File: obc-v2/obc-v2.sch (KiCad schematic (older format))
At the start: 57 parts

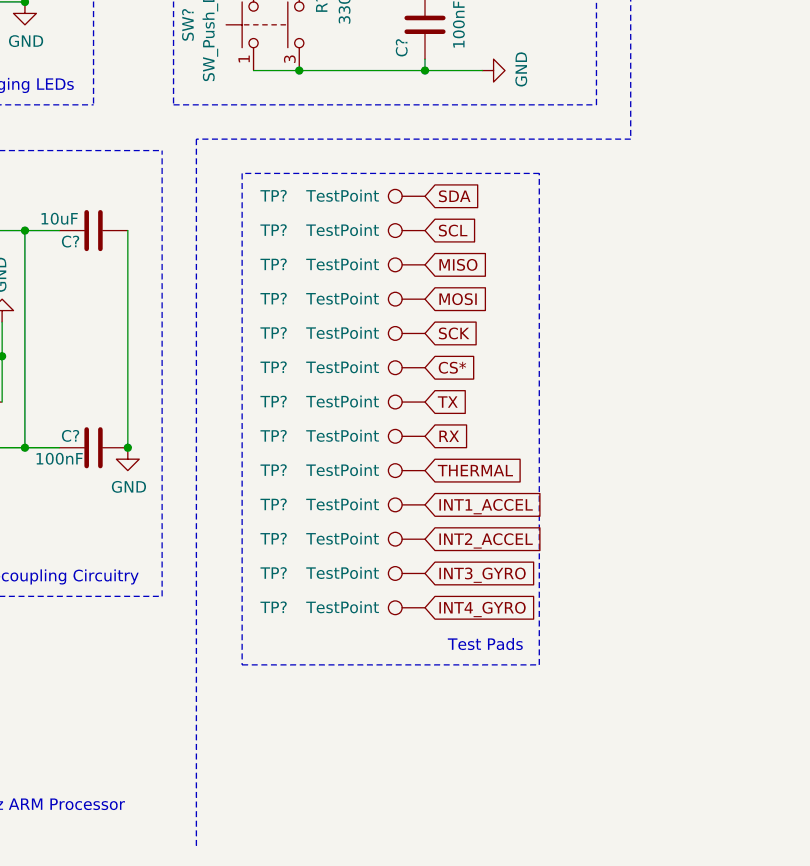
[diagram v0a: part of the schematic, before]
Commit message: obc-v2: Add test pads
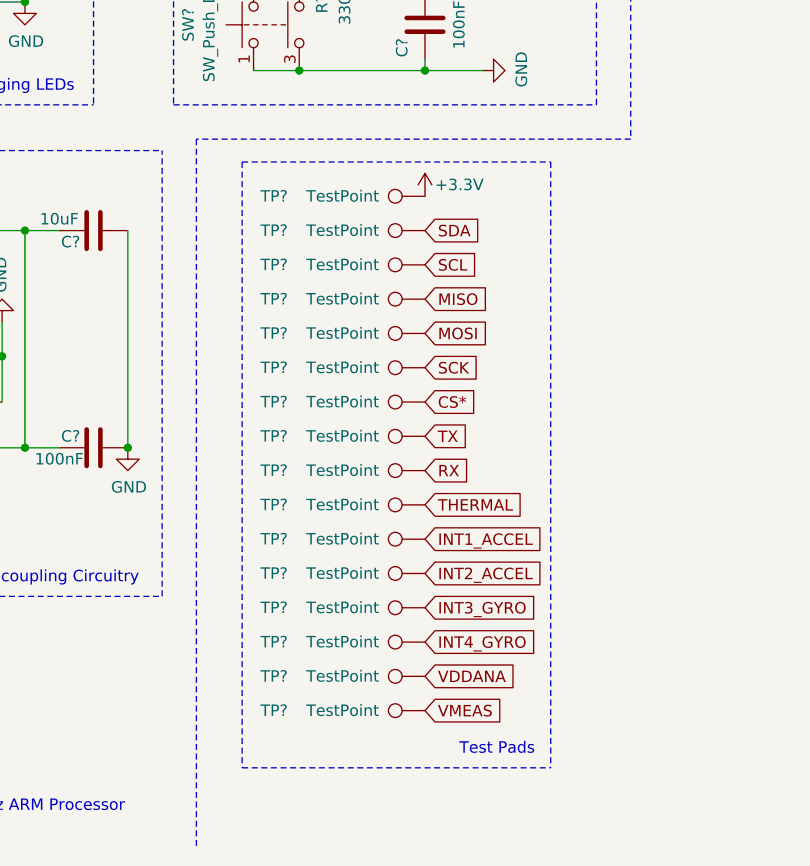
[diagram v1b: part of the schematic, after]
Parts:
- added TP? (x3): TestPoint, symbol Connector:TestPoint
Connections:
- net +3V3: now also TP?.1
- net VDDANA: now also TP?.1
- net VMEAS: now also TP?.1
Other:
- moved on the sheet: TP?
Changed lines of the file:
@@
 L Connector:TestPoint TP?
 U 1 1 6165481C
+P 4200 5100
+F 0 "TP?" V 4200 5700 50  0000 L CNN
+F 1 "TestPoint" V 4200 5300 50  0000 L CNN
+F 2 "" H 4400 5100 50  0001 C CNN
+F 3 "" H 4400 5100 50  0001 C CNN
+	1    4200 5100
+	0    -1   -1   0
+$EndComp
+Text GLabel 4200 5100 2    50   Input ~ 0
+SDA
+$Comp
+L Connector:TestPoint TP?
+U 1 1 616A4E70
+P 4200 5250
+F 0 "TP?" V 4200 5850 50  0000 L CNN
+F 1 "TestPoint" V 4200 5450 50  0000 L CNN
+F 2 "" H 4400 5250 50  0001 C CNN
+F 3 "" H 4400 5250 50  0001 C CNN
+	1    4200 5250
+	0    -1   -1   0
+$EndComp
+Text GLabel 4200 5250 2    50   Input ~ 0
+SCL
+$Comp
+L Connector:TestPoint TP?
+U 1 1 616A8E8A
+P 4200 5400
+F 0 "TP?" V 4200 6000 50  0000 L CNN
+F 1 "TestPoint" V 4200 5600 50  0000 L CNN
+F 2 "" H 4400 5400 50  0001 C CNN
+F 3 "" H 4400 5400 50  0001 C CNN
+	1    4200 5400
+	0    -1   -1   0
+$EndComp
+Text GLabel 4200 5400 2    50   Input ~ 0
+MISO
+$Comp
+L Connector:TestPoint TP?
+U 1 1 616A8E91
+P 4200 5550
+F 0 "TP?" V 4200 6150 50  0000 L CNN
+F 1 "TestPoint" V 4200 5750 50  0000 L CNN
+F 2 "" H 4400 5550 50  0001 C CNN
+F 3 "" H 4400 5550 50  0001 C CNN
+	1    4200 5550
+	0    -1   -1   0
+$EndComp
+Text GLabel 4200 5550 2    50   Input ~ 0
+MOSI
+$Comp
+L Connector:TestPoint TP?
+U 1 1 616AD625
+P 4200 5700
+F 0 "TP?" V 4200 6300 50  0000 L CNN
+F 1 "TestPoint" V 4200 5900 50  0000 L CNN
+F 2 "" H 4400 5700 50  0001 C CNN
+F 3 "" H 4400 5700 50  0001 C CNN
+	1    4200 5700
+	0    -1   -1   0
+$EndComp
+Text GLabel 4200 5700 2    50   Input ~ 0
+SCK
+$Comp
+L Connector:TestPoint TP?
+U 1 1 616AD62C
+P 4200 5850
+F 0 "TP?" V 4200 6450 50  0000 L CNN
+F 1 "TestPoint" V 4200 6050 50  0000 L CNN
+F 2 "" H 4400 5850 50  0001 C CNN
+F 3 "" H 4400 5850 50  0001 C CNN
+	1    4200 5850
+	0    -1   -1   0
+$EndComp
+Text GLabel 4200 5850 2    50   Input ~ 0
+CS*
+$Comp
+L Connector:TestPoint TP?
+U 1 1 616AD633
+P 4200 6000
+F 0 "TP?" V 4200 6600 50  0000 L CNN
+F 1 "TestPoint" V 4200 6200 50  0000 L CNN
+F 2 "" H 4400 6000 50  0001 C CNN
+F 3 "" H 4400 6000 50  0001 C CNN
+	1    4200 6000
+	0    -1   -1   0
+$EndComp
+Text GLabel 4200 6000 2    50   Input ~ 0
+TX
+$Comp
+L Connector:TestPoint TP?
+U 1 1 616AD63A
+P 4200 6150
+F 0 "TP?" V 4200 6750 50  0000 L CNN
+F 1 "TestPoint" V 4200 6350 50  0000 L CNN
+F 2 "" H 4400 6150 50  0001 C CNN
+F 3 "" H 4400 6150 50  0001 C CNN
+	1    4200 6150
+	0    -1   -1   0
+$EndComp
+Text GLabel 4200 6150 2    50   Input ~ 0
+RX
+$Comp
+L Connector:TestPoint TP?
+U 1 1 616B2BB2
+P 4200 6300
+F 0 "TP?" V 4200 6900 50  0000 L CNN
+F 1 "TestPoint" V 4200 6500 50  0000 L CNN
+F 2 "" H 4400 6300 50  0001 C CNN
+F 3 "" H 4400 6300 50  0001 C CNN
+	1    4200 6300
+	0    -1   -1   0
+$EndComp
+Text GLabel 4200 6300 2    50   Input ~ 0
+THERMAL
+$Comp
+L Connector:TestPoint TP?
+U 1 1 616B2BB9
+P 4200 6450
+F 0 "TP?" V 4200 7050 50  0000 L CNN
+F 1 "TestPoint" V 4200 6650 50  0000 L CNN
+F 2 "" H 4400 6450 50  0001 C CNN
+F 3 "" H 4400 6450 50  0001 C CNN
+	1    4200 6450
+	0    -1   -1   0
+$EndComp
+Text GLabel 4200 6450 2    50   Input ~ 0
+INT1_ACCEL
+$Comp
+L Connector:TestPoint TP?
+U 1 1 616B2BC0
+P 4200 6600
+F 0 "TP?" V 4200 7200 50  0000 L CNN
+F 1 "TestPoint" V 4200 6800 50  0000 L CNN
+F 2 "" H 4400 6600 50  0001 C CNN
+F 3 "" H 4400 6600 50  0001 C CNN
+	1    4200 6600
+	0    -1   -1   0
+$EndComp
+Text GLabel 4200 6600 2    50   Input ~ 0
+INT2_ACCEL
+$Comp
+L Connector:TestPoint TP?
+U 1 1 616B2BC7
+P 4200 6750
+F 0 "TP?" V 4200 7350 50  0000 L CNN
+F 1 "TestPoint" V 4200 6950 50  0000 L CNN
+F 2 "" H 4400 6750 50  0001 C CNN
+F 3 "" H 4400 6750 50  0001 C CNN
+	1    4200 6750
+	0    -1   -1   0
+$EndComp
+Text GLabel 4200 6750 2    50   Input ~ 0
+INT3_GYRO
+$Comp
+L Connector:TestPoint TP?
+U 1 1 616B2BCE
+P 4200 6900
+F 0 "TP?" V 4200 7500 50  0000 L CNN
+F 1 "TestPoint" V 4200 7100 50  0000 L CNN
+F 2 "" H 4400 6900 50  0001 C CNN
+F 3 "" H 4400 6900 50  0001 C CNN
+	1    4200 6900
+	0    -1   -1   0
+$EndComp
+Text GLabel 4200 6900 2    50   Input ~ 0
+INT4_GYRO
+Text Notes 4350 7400 0    50   ~ 0
+Test Pads
+$Comp
+L Connector:TestPoint TP?
+U 1 1 61552B8D
 P 4200 4950
 F 0 "TP?" V 4200 5550 50  0000 L CNN
@@
 	0    -1   -1   0
 $EndComp
-Text GLabel 4200 4950 2    50   Input ~ 0
-SDA
-$Comp
-L Connector:TestPoint TP?
-U 1 1 616A4E70
-P 4200 5100
-F 0 "TP?" V 4200 5700 50  0000 L CNN
-F 1 "TestPoint" V 4200 5300 50  0000 L CNN
-F 2 "" H 4400 5100 50  0001 C CNN
-F 3 "" H 4400 5100 50  0001 C CNN
-	1    4200 5100
-	0    -1   -1   0
-$EndComp
-Text GLabel 4200 5100 2    50   Input ~ 0
-SCL
-$Comp
-L Connector:TestPoint TP?
-U 1 1 616A8E8A
-P 4200 5250
-F 0 "TP?" V 4200 5850 50  0000 L CNN
-F 1 "TestPoint" V 4200 5450 50  0000 L CNN
-F 2 "" H 4400 5250 50  0001 C CNN
-F 3 "" H 4400 5250 50  0001 C CNN
-	1    4200 5250
-	0    -1   -1   0
-$EndComp
-Text GLabel 4200 5250 2    50   Input ~ 0
-MISO
-$Comp
-L Connector:TestPoint TP?
-U 1 1 616A8E91
-P 4200 5400
-F 0 "TP?" V 4200 6000 50  0000 L CNN
-F 1 "TestPoint" V 4200 5600 50  0000 L CNN
-F 2 "" H 4400 5400 50  0001 C CNN
-F 3 "" H 4400 5400 50  0001 C CNN
-	1    4200 5400
-	0    -1   -1   0
-$EndComp
-Text GLabel 4200 5400 2    50   Input ~ 0
-MOSI
-$Comp
-L Connector:TestPoint TP?
-U 1 1 616AD625
-P 4200 5550
-F 0 "TP?" V 4200 6150 50  0000 L CNN
-F 1 "TestPoint" V 4200 5750 50  0000 L CNN
-F 2 "" H 4400 5550 50  0001 C CNN
-F 3 "" H 4400 5550 50  0001 C CNN
-	1    4200 5550
-	0    -1   -1   0
-$EndComp
-Text GLabel 4200 5550 2    50   Input ~ 0
-SCK
-$Comp
-L Connector:TestPoint TP?
-U 1 1 616AD62C
-P 4200 5700
-F 0 "TP?" V 4200 6300 50  0000 L CNN
-F 1 "TestPoint" V 4200 5900 50  0000 L CNN
-F 2 "" H 4400 5700 50  0001 C CNN
-F 3 "" H 4400 5700 50  0001 C CNN
-	1    4200 5700
-	0    -1   -1   0
-$EndComp
-Text GLabel 4200 5700 2    50   Input ~ 0
-CS*
-$Comp
-L Connector:TestPoint TP?
-U 1 1 616AD633
-P 4200 5850
-F 0 "TP?" V 4200 6450 50  0000 L CNN
-F 1 "TestPoint" V 4200 6050 50  0000 L CNN
-F 2 "" H 4400 5850 50  0001 C CNN
-F 3 "" H 4400 5850 50  0001 C CNN
-	1    4200 5850
-	0    -1   -1   0
-$EndComp
-Text GLabel 4200 5850 2    50   Input ~ 0
-TX
-$Comp
-L Connector:TestPoint TP?
-U 1 1 616AD63A
-P 4200 6000
-F 0 "TP?" V 4200 6600 50  0000 L CNN
-F 1 "TestPoint" V 4200 6200 50  0000 L CNN
-F 2 "" H 4400 6000 50  0001 C CNN
-F 3 "" H 4400 6000 50  0001 C CNN
-	1    4200 6000
-	0    -1   -1   0
-$EndComp
-Text GLabel 4200 6000 2    50   Input ~ 0
-RX
-$Comp
-L Connector:TestPoint TP?
-U 1 1 616B2BB2
-P 4200 6150
-F 0 "TP?" V 4200 6750 50  0000 L CNN
-F 1 "TestPoint" V 4200 6350 50  0000 L CNN
-F 2 "" H 4400 6150 50  0001 C CNN
-F 3 "" H 4400 6150 50  0001 C CNN
-	1    4200 6150
-	0    -1   -1   0
-$EndComp
-Text GLabel 4200 6150 2    50   Input ~ 0
-THERMAL
-$Comp
-L Connector:TestPoint TP?
-U 1 1 616B2BB9
-P 4200 6300
-F 0 "TP?" V 4200 6900 50  0000 L CNN
-F 1 "TestPoint" V 4200 6500 50  0000 L CNN
-F 2 "" H 4400 6300 50  0001 C CNN
-F 3 "" H 4400 6300 50  0001 C CNN
-	1    4200 6300
-	0    -1   -1   0
-$EndComp
-Text GLabel 4200 6300 2    50   Input ~ 0
-INT1_ACCEL
-$Comp
-L Connector:TestPoint TP?
-U 1 1 616B2BC0
-P 4200 6450
-F 0 "TP?" V 4200 7050 50  0000 L CNN
-F 1 "TestPoint" V 4200 6650 50  0000 L CNN
-F 2 "" H 4400 6450 50  0001 C CNN
-F 3 "" H 4400 6450 50  0001 C CNN
-	1    4200 6450
-	0    -1   -1   0
-$EndComp
-Text GLabel 4200 6450 2    50   Input ~ 0
-INT2_ACCEL
-$Comp
-L Connector:TestPoint TP?
-U 1 1 616B2BC7
-P 4200 6600
-F 0 "TP?" V 4200 7200 50  0000 L CNN
-F 1 "TestPoint" V 4200 6800 50  0000 L CNN
-F 2 "" H 4400 6600 50  0001 C CNN
-F 3 "" H 4400 6600 50  0001 C CNN
-	1    4200 6600
-	0    -1   -1   0
-$EndComp
-Text GLabel 4200 6600 2    50   Input ~ 0
-INT3_GYRO
-$Comp
-L Connector:TestPoint TP?
-U 1 1 616B2BCE
-P 4200 6750
-F 0 "TP?" V 4200 7350 50  0000 L CNN
-F 1 "TestPoint" V 4200 6950 50  0000 L CNN
-F 2 "" H 4400 6750 50  0001 C CNN
-F 3 "" H 4400 6750 50  0001 C CNN
-	1    4200 6750
-	0    -1   -1   0
-$EndComp
-Text GLabel 4200 6750 2    50   Input ~ 0
-INT4_GYRO
-Text Notes 4300 6950 0    50   ~ 0
-Test Pads
-Wire Notes Line
-	4700 7000 4700 4850
-Wire Notes Line
-	4700 4850 3400 4850
-Wire Notes Line
-	3400 4850 3400 7000
-Wire Notes Line
-	3400 7000 4700 7000
+$Comp
+L Connector:TestPoint TP?
+U 1 1 61552B94
+P 4200 7050
+F 0 "TP?" V 4200 7650 50  0000 L CNN
+F 1 "TestPoint" V 4200 7250 50  0000 L CNN
+F 2 "" H 4400 7050 50  0001 C CNN
+F 3 "" H 4400 7050 50  0001 C CNN
+	1    4200 7050
+	0    -1   -1   0
+$EndComp
+Text GLabel 4200 7050 2    50   Input ~ 0
+VDDANA
+$Comp
+L Connector:TestPoint TP?
+U 1 1 61552B9B
+P 4200 7200
+F 0 "TP?" V 4200 7800 50  0000 L CNN
+F 1 "TestPoint" V 4200 7400 50  0000 L CNN
+F 2 "" H 4400 7200 50  0001 C CNN
+F 3 "" H 4400 7200 50  0001 C CNN
+	1    4200 7200
+	0    -1   -1   0
+$EndComp
+Text GLabel 4200 7200 2    50   Input ~ 0
+VMEAS
+$Comp
+L obc-v2-rescue:+3.3V-power #PWR?
+U 1 1 6155F497
+P 4200 4950
+F 0 "#PWR?" H 4200 4800 50  0001 C CNN
+F 1 "+3.3V" H 4350 5000 50  0000 C CNN
+F 2 "" H 4200 4950 50  0001 C CNN
+F 3 "" H 4200 4950 50  0001 C CNN
+	1    4200 4950
+	1    0    0    -1
+$EndComp
+Wire Notes Line
+	3400 4800 4750 4800
+Wire Notes Line
+	4750 4800 4750 7450
+Wire Notes Line
+	3400 7450 4750 7450
+Wire Notes Line
+	3400 4800 3400 7450
 $EndSCHEMATC
